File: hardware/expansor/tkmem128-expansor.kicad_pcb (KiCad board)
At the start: 2 copper layers, 78.7 x 45 mm, 3 parts, among them J1 Terminais do conector, J2 Passagem

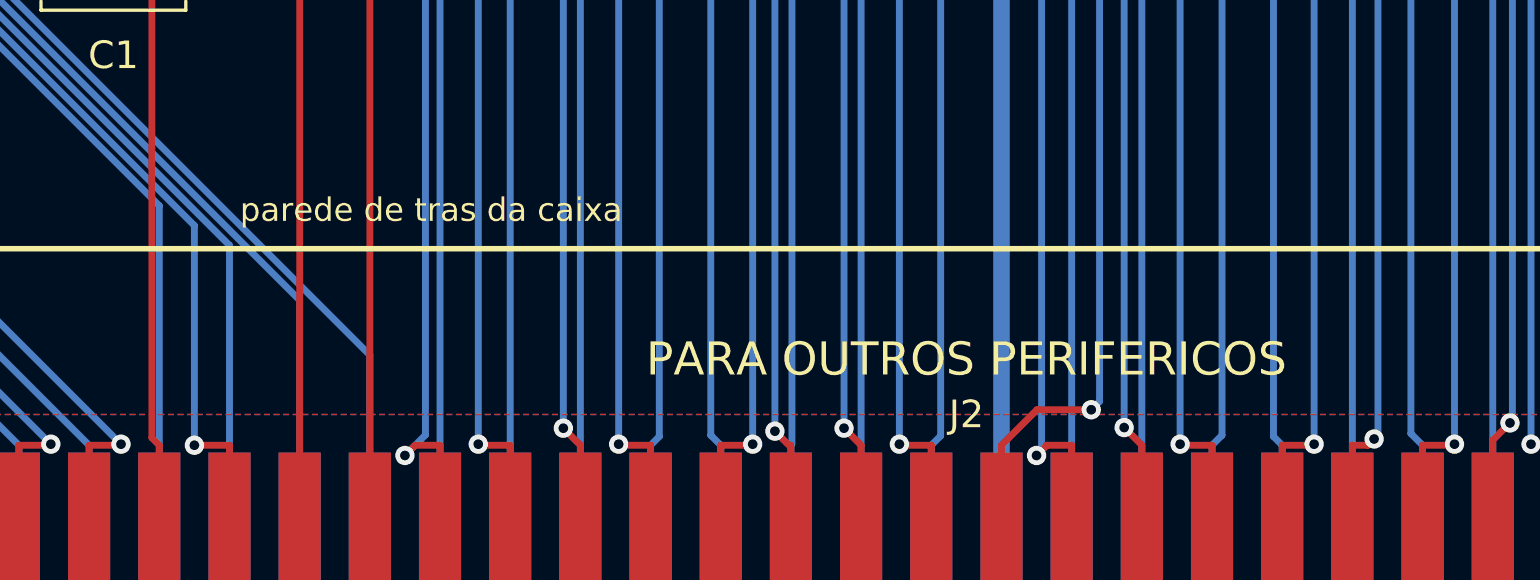
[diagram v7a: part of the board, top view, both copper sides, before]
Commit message: Numeracao do conector tambem no lado dos componentes da principal
J1 fica em B.Cu - e o unico componente do lado do cobre - e toda a serigrafia
dele morava so em B.Silkscreen, o lado onde o conector e soldado. Mas o lado
dos componentes e onde a TIRA DE EXPANSAO e soldada, nos mesmos terminais que
atravessam a placa: quem monta precisa da numeracao la tambem.

O conector e THT, entao cada pino existe nas duas faces na mesma coluna e os
mesmos rotulos valem para as duas, nas mesmas coordenadas. Muda so qual ponta
aparece a esquerda, porque e a mesma placa vista do outro lado.

De quebra, o contorno do corpo do conector descia ate y=67,23 numa placa de
66,04 mm: 1,19 mm de serigrafia fora da placa e dois tracos verticais cruzando
a aresta - os 3 avisos de silk_edge_clearance que a principal carregava. O
mesmo tratamento que a tira levou: U aberto para a aresta, parando 0,3 mm antes
dela. O contorno cheio continua correto na biblioteca, porque o corpo de um
conector de borda avanca mesmo alem da placa; aparar e decisao de placa, nao de
footprint.

DRC da principal: de 5 violacoes para 2. As duas que sobram sao starved_thermal
nos pads de GND de C4 e C6, anteriores a isto e de outra natureza.

confere_alinhamento.py ja cobre a placa principal na verificacao de rotulos, e
segue passando nas duas.

Co-Authored-By: Claude Opus 5 <noreply@anthropic.com>
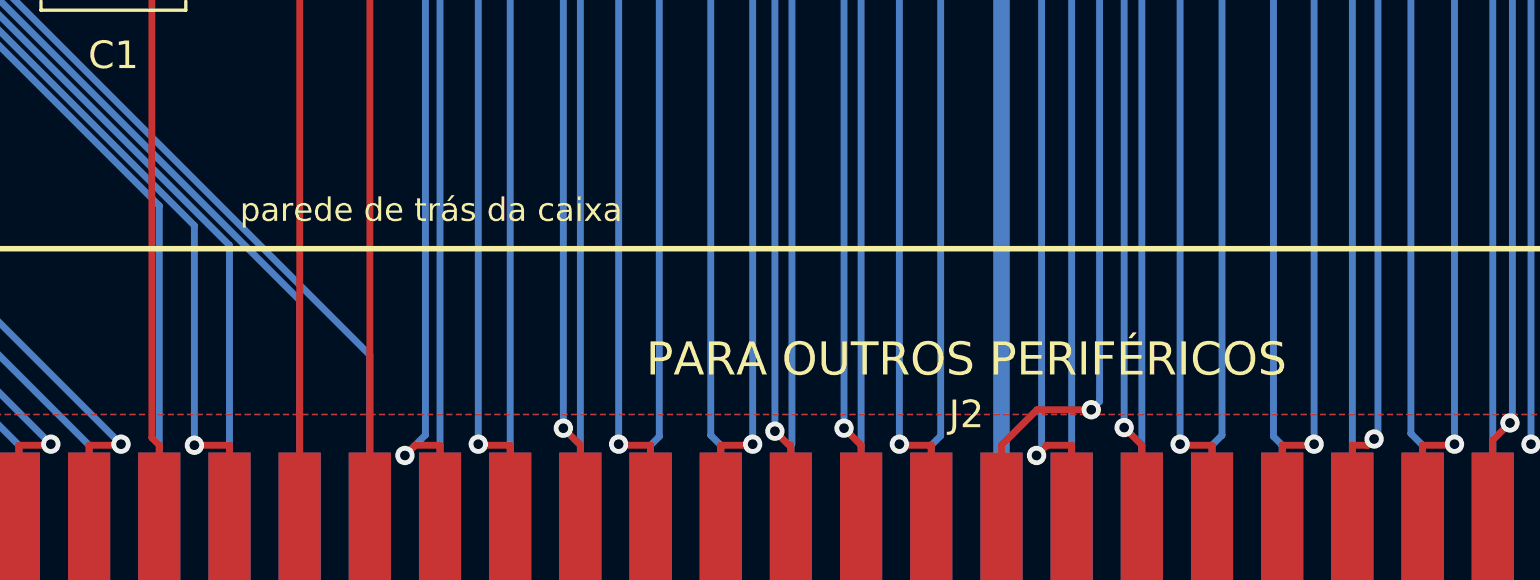
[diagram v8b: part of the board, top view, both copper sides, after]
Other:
- board text added: "PARA OUTROS PERIFÉRICOS"
- board text added: "parede de trás da caixa"
- board text removed: "PARA OUTROS PERIFERICOS"
- board text removed: "parede de tras da caixa"
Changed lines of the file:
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@@
 		(layer "Edge.Cuts")
 	)
-	(gr_text "parede de tras da caixa"
+	(gr_text "parede de trás da caixa"
 		(at 20 28.6 0)
 		(layer "F.SilkS")
@@
 		)
 	)
-	(gr_text "PARA OUTROS PERIFERICOS"
+	(gr_text "PARA OUTROS PERIFÉRICOS"
 		(at 39.37 34 0)
 		(layer "F.SilkS")
